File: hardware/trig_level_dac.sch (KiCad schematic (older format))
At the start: 28 parts, among them U701 DAC7563SDSCR, U702 OPA2140

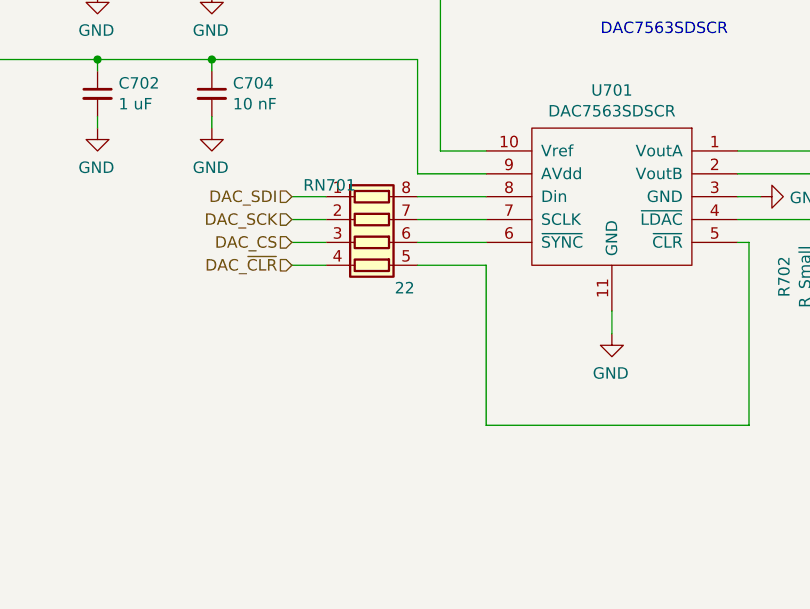
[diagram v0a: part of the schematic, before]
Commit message: work on tdr component placement
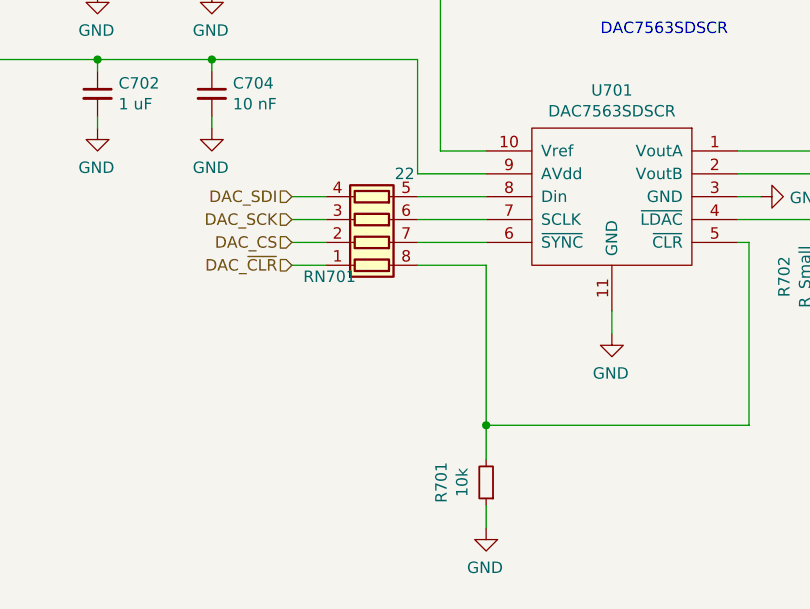
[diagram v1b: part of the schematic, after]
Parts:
- added R701: 10k, Resistors_SMD:R_0402, symbol Device:R_Small
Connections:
- net DAC_CS: now also RN701.2 (R2.1); no longer RN701.3 (R3.1)
- net DAC_SCK: now also RN701.3 (R3.1); no longer RN701.2 (R2.1)
- net DAC_SDI: now also RN701.4 (R4.1); no longer RN701.1 (R1.1)
- net DAC_~CLR: now also RN701.1 (R1.1); no longer RN701.4 (R4.1)
- net GND: now also R701.1
- net at U701.5 (~CLR): now also RN701.8 (R1.2), R701.2; no longer RN701.5 (R4.2)
- net at U701.6 (~SYNC): now also RN701.7 (R2.2); no longer RN701.6 (R3.2)
- net at U701.7 (SCLK): now also RN701.6 (R3.2); no longer RN701.7 (R2.2)
- net at U701.8 (Din): now also RN701.5 (R4.2); no longer RN701.8 (R1.2)
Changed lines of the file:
@@
 L Device:R_Pack04 RN?
 U 1 1 5C28A2D7
-P 2900 4800
+P 2900 4700
 AR Path="/5BC6A656/5C28A2D7" Ref="RN?"  Part="1"
 AR Path="/5BC64E97/5C28A2D7" Ref="RN?"  Part="1"
 AR Path="/5C262FB6/5C28A2D7" Ref="RN701"  Part="1"
-F 0 "RN701" V 2650 4500 50  0000 L CNN
-F 1 "22" V 3100 4900 50  0000 L CNN
-F 2 "Resistors_SMD:R_Array_Convex_4x0402" V 3175 4800 50  0001 C CNN
-F 3 "~" H 2900 4800 50  0001 C CNN
-	1    2900 4800
-	0    1    1    0
+F 0 "RN701" V 2650 4400 50  0000 L CNN
+F 1 "22" V 3100 4800 50  0000 L CNN
+F 2 "Resistors_SMD:R_Array_Convex_4x0402" V 3175 4700 50  0001 C CNN
+F 3 "~" H 2900 4700 50  0001 C CNN
+	1    2900 4700
+	0    1    -1   0
 $EndComp
 Wire Wire Line
@@
 Text HLabel 2550 4900 0    50   Input ~ 0
 DAC_~CLR
+$Comp
+L Device:R_Small R701
+U 1 1 5C36F4E9
+P 3400 5850
+F 0 "R701" V 3596 5850 50  0000 C CNN
+F 1 "10k" V 3505 5850 50  0000 C CNN
+F 2 "Resistors_SMD:R_0402" H 3400 5850 50  0001 C CNN
+F 3 "~" H 3400 5850 50  0001 C CNN
+	1    3400 5850
+	-1   0    0    1
+$EndComp
+$Comp
+L power:GND #PWR0149
+U 1 1 5C36F5ED
+P 3400 6050
+F 0 "#PWR0149" H 3400 5800 50  0001 C CNN
+F 1 "GND" H 3405 5877 50  0000 C CNN
+F 2 "" H 3400 6050 50  0001 C CNN
+F 3 "" H 3400 6050 50  0001 C CNN
+	1    3400 6050
+	-1   0    0    -1
+$EndComp
+Wire Wire Line
+	3400 5600 3400 5750
+Connection ~ 3400 5600
+Wire Wire Line
+	3400 5950 3400 6050
 $EndSCHEMATC

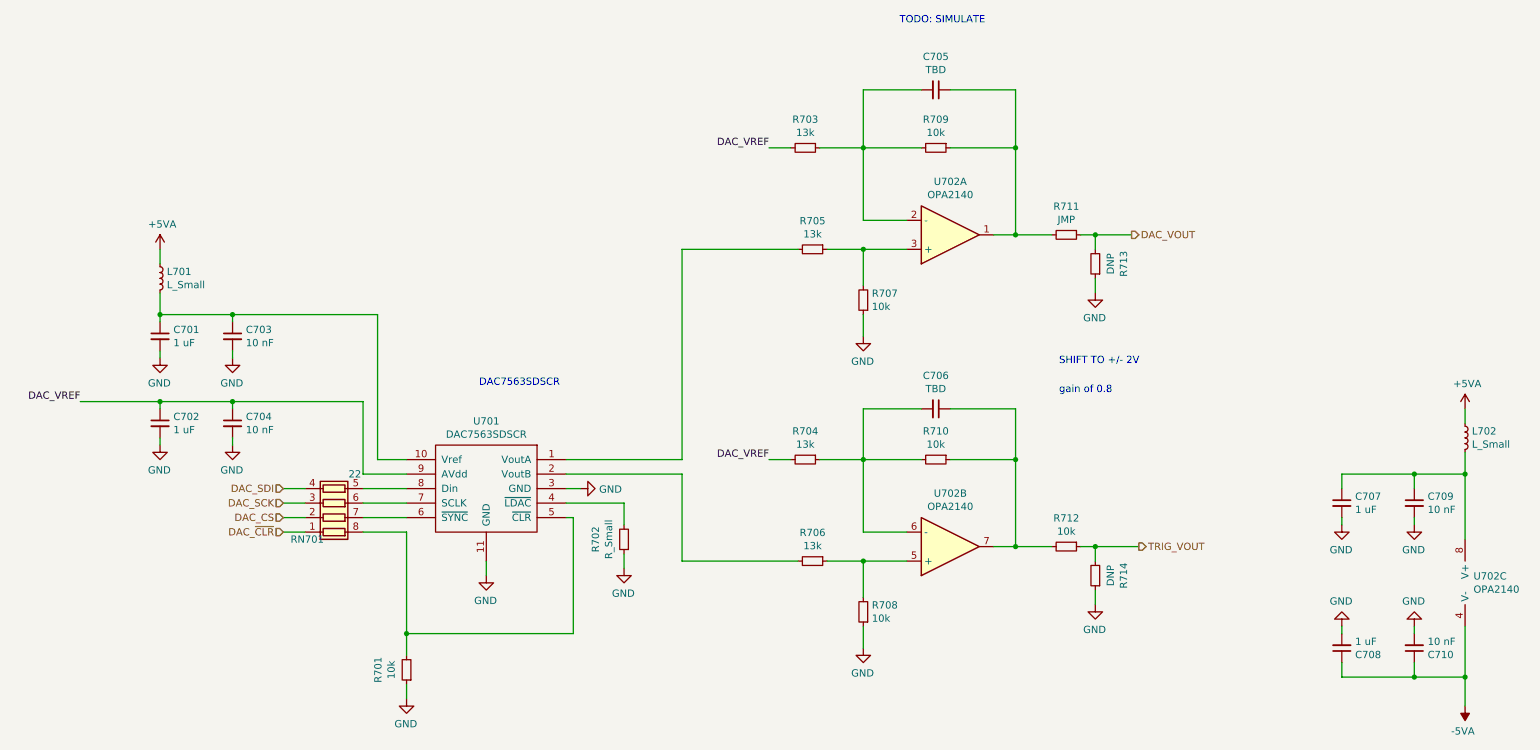
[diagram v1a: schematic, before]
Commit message: schematic cleanup, BOM consolidation
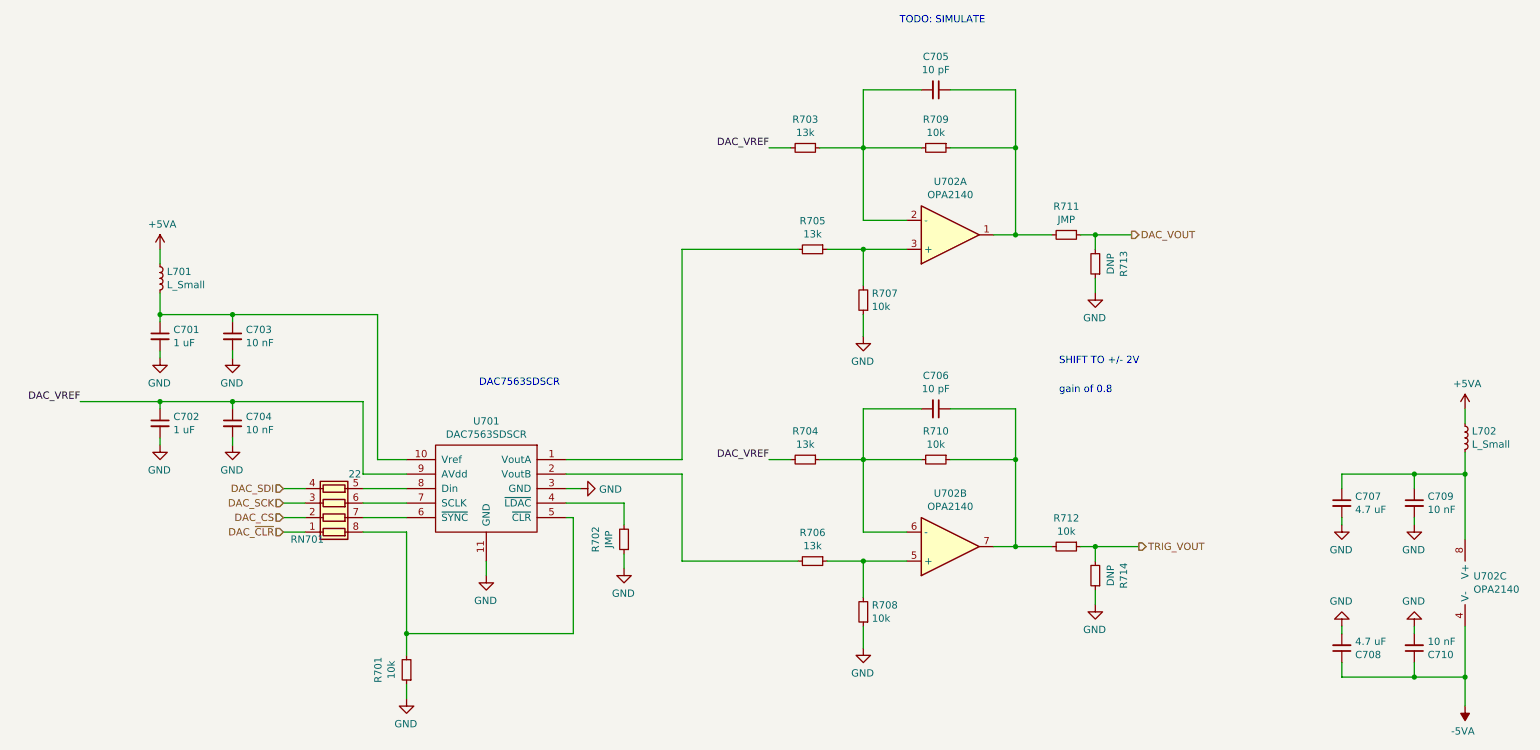
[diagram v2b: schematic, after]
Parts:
- C705, C706: value TBD -> 10 pF
- C707, C708: value 1 uF -> 4.7 uF
- R702: value R_Small -> JMP
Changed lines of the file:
@@
 P 4900 4950
 F 0 "R702" V 5096 4950 50  0000 C CNN
-F 1 "R_Small" V 5005 4950 50  0000 C CNN
+F 1 "JMP" V 5005 4950 50  0000 C CNN
 F 2 "Resistors_SMD:R_0402" H 4900 4950 50  0001 C CNN
 F 3 "~" H 4900 4950 50  0001 C CNN
@@
 P 9850 4700
 F 0 "C707" H 9942 4746 50  0000 L CNN
-F 1 "1 uF" H 9942 4655 50  0000 L CNN
+F 1 "4.7 uF" H 9942 4655 50  0000 L CNN
 F 2 "Capacitors_SMD:C_0603" H 9850 4700 50  0001 C CNN
 F 3 "~" H 9850 4700 50  0001 C CNN
@@
 P 9850 5700
 F 0 "C708" H 9942 5746 50  0000 L CNN
-F 1 "1 uF" H 9942 5655 50  0000 L CNN
+F 1 "4.7 uF" H 9942 5655 50  0000 L CNN
 F 2 "Capacitors_SMD:C_0603" H 9850 5700 50  0001 C CNN
 F 3 "~" H 9850 5700 50  0001 C CNN
@@
 P 7050 1850
 F 0 "C705" V 6821 1850 50  0000 C CNN
-F 1 "TBD" V 6912 1850 50  0000 C CNN
+F 1 "10 pF" V 6912 1850 50  0000 C CNN
 F 2 "Capacitors_SMD:C_0402" H 7050 1850 50  0001 C CNN
 F 3 "~" H 7050 1850 50  0001 C CNN
@@
 P 7050 4050
 F 0 "C706" V 6821 4050 50  0000 C CNN
-F 1 "TBD" V 6912 4050 50  0000 C CNN
+F 1 "10 pF" V 6912 4050 50  0000 C CNN
 F 2 "Capacitors_SMD:C_0402" H 7050 4050 50  0001 C CNN
 F 3 "~" H 7050 4050 50  0001 C CNN

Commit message: assigned pins for tdr beaglebone bitbang driver
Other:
- note added: "TODO: WHAT IS THE STATE OF THIS AT STARTUP?"
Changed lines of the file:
@@
 Wire Wire Line
 	3400 5950 3400 6050
+Text Notes 8200 4300 0    50   ~ 0
+TODO: WHAT IS THE STATE OF THIS AT STARTUP?
 $EndSCHEMATC

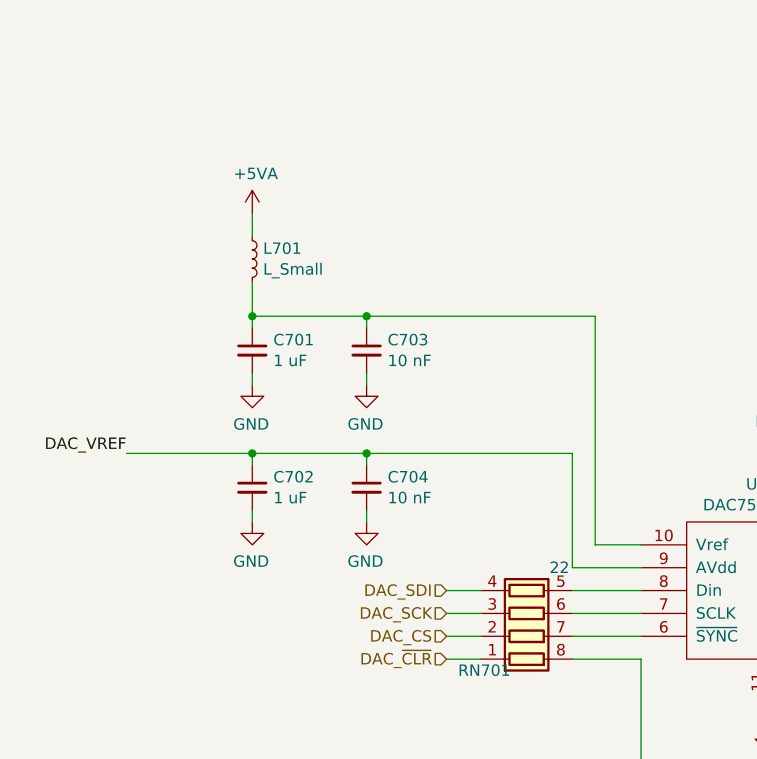
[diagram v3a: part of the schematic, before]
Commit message: fixed U401 and U601 output termination, tdr works, added first sweep of output pulse to README
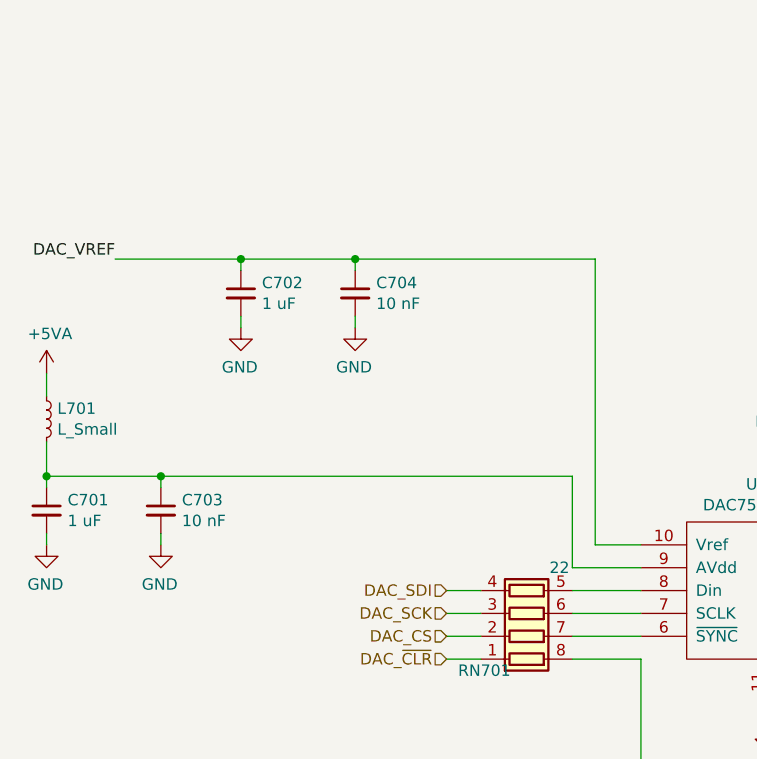
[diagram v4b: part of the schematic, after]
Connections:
- net DAC_VREF: now also U701.10 (Vref); no longer U701.9 (AVdd)
- net at C701.1, C703.1, L701.2: now also U701.9 (AVdd); no longer U701.10 (Vref)
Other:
- moved on the sheet: C701, C702, C703, C704, L701
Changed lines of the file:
@@
 L Device:C_Small C703
 U 1 1 5C28C367
-P 2200 3550
-F 0 "C703" H 2292 3596 50  0000 L CNN
-F 1 "10 nF" H 2292 3505 50  0000 L CNN
-F 2 "Capacitors_SMD:C_0402" H 2200 3550 50  0001 C CNN
-F 3 "~" H 2200 3550 50  0001 C CNN
-	1    2200 3550
+P 1300 4250
+F 0 "C703" H 1392 4296 50  0000 L CNN
+F 1 "10 nF" H 1392 4205 50  0000 L CNN
+F 2 "Capacitors_SMD:C_0402" H 1300 4250 50  0001 C CNN
+F 3 "~" H 1300 4250 50  0001 C CNN
+	1    1300 4250
 	1    0    0    -1
 $EndComp
@@
 L Device:C_Small C701
 U 1 1 5C28C3DD
-P 1700 3550
-F 0 "C701" H 1792 3596 50  0000 L CNN
-F 1 "1 uF" H 1792 3505 50  0000 L CNN
-F 2 "Capacitors_SMD:C_0402" H 1700 3550 50  0001 C CNN
-F 3 "~" H 1700 3550 50  0001 C CNN
-	1    1700 3550
+P 800 4250
+F 0 "C701" H 892 4296 50  0000 L CNN
+F 1 "1 uF" H 892 4205 50  0000 L CNN
+F 2 "Capacitors_SMD:C_0402" H 800 4250 50  0001 C CNN
+F 3 "~" H 800 4250 50  0001 C CNN
+	1    800  4250
 	1    0    0    -1
 $EndComp
@@
 L power:GND #PWR0282
 U 1 1 5C28C8E7
-P 2200 3700
-F 0 "#PWR0282" H 2200 3450 50  0001 C CNN
-F 1 "GND" H 2205 3527 50  0000 C CNN
-F 2 "" H 2200 3700 50  0001 C CNN
-F 3 "" H 2200 3700 50  0001 C CNN
-	1    2200 3700
-	-1   0    0    -1
-$EndComp
-Wire Wire Line
-	1700 3400 2200 3400
-Connection ~ 1700 3400
-Wire Wire Line
-	1700 3400 1700 3450
-Wire Wire Line
-	2200 3400 2200 3450
-Wire Wire Line
-	2200 3650 2200 3700
+P 1300 4400
+F 0 "#PWR0282" H 1300 4150 50  0001 C CNN
+F 1 "GND" H 1305 4227 50  0000 C CNN
+F 2 "" H 1300 4400 50  0001 C CNN
+F 3 "" H 1300 4400 50  0001 C CNN
+	1    1300 4400
+	-1   0    0    -1
+$EndComp
+Wire Wire Line
+	800  4100 1300 4100
+Connection ~ 800  4100
+Wire Wire Line
+	800  4100 800  4150
+Wire Wire Line
+	1300 4100 1300 4150
+Wire Wire Line
+	1300 4350 1300 4400
 $Comp
 L power:GND #PWR0283
 U 1 1 5C28D08C
-P 1700 3700
-F 0 "#PWR0283" H 1700 3450 50  0001 C CNN
-F 1 "GND" H 1705 3527 50  0000 C CNN
-F 2 "" H 1700 3700 50  0001 C CNN
-F 3 "" H 1700 3700 50  0001 C CNN
-	1    1700 3700
-	-1   0    0    -1
-$EndComp
-Wire Wire Line
-	1700 3650 1700 3700
+P 800 4400
+F 0 "#PWR0283" H 800 4150 50  0001 C CNN
+F 1 "GND" H 805 4227 50  0000 C CNN
+F 2 "" H 800 4400 50  0001 C CNN
+F 3 "" H 800 4400 50  0001 C CNN
+	1    800  4400
+	-1   0    0    -1
+$EndComp
+Wire Wire Line
+	800  4350 800  4400
 $Comp
 L Device:C_Small C704
 U 1 1 5C28D757
-P 2200 4150
-F 0 "C704" H 2292 4196 50  0000 L CNN
-F 1 "10 nF" H 2292 4105 50  0000 L CNN
-F 2 "Capacitors_SMD:C_0402" H 2200 4150 50  0001 C CNN
-F 3 "~" H 2200 4150 50  0001 C CNN
-	1    2200 4150
+P 2150 3300
+F 0 "C704" H 2242 3346 50  0000 L CNN
+F 1 "10 nF" H 2242 3255 50  0000 L CNN
+F 2 "Capacitors_SMD:C_0402" H 2150 3300 50  0001 C CNN
+F 3 "~" H 2150 3300 50  0001 C CNN
+	1    2150 3300
 	1    0    0    -1
 $EndComp
@@
 L Device:C_Small C702
 U 1 1 5C28D75E
-P 1700 4150
-F 0 "C702" H 1792 4196 50  0000 L CNN
-F 1 "1 uF" H 1792 4105 50  0000 L CNN
-F 2 "Capacitors_SMD:C_0402" H 1700 4150 50  0001 C CNN
-F 3 "~" H 1700 4150 50  0001 C CNN
-	1    1700 4150
+P 1650 3300
+F 0 "C702" H 1742 3346 50  0000 L CNN
+F 1 "1 uF" H 1742 3255 50  0000 L CNN
+F 2 "Capacitors_SMD:C_0402" H 1650 3300 50  0001 C CNN
+F 3 "~" H 1650 3300 50  0001 C CNN
+	1    1650 3300
 	1    0    0    -1
 $EndComp
@@
 L power:GND #PWR0284
 U 1 1 5C28D765
-P 2200 4300
-F 0 "#PWR0284" H 2200 4050 50  0001 C CNN
-F 1 "GND" H 2205 4127 50  0000 C CNN
-F 2 "" H 2200 4300 50  0001 C CNN
-F 3 "" H 2200 4300 50  0001 C CNN
-	1    2200 4300
-	-1   0    0    -1
-$EndComp
-Wire Wire Line
-	1700 4000 2200 4000
-Wire Wire Line
-	1700 4000 1700 4050
-Wire Wire Line
-	2200 4000 2200 4050
-Wire Wire Line
-	2200 4250 2200 4300
+P 2150 3450
+F 0 "#PWR0284" H 2150 3200 50  0001 C CNN
+F 1 "GND" H 2155 3277 50  0000 C CNN
+F 2 "" H 2150 3450 50  0001 C CNN
+F 3 "" H 2150 3450 50  0001 C CNN
+	1    2150 3450
+	-1   0    0    -1
+$EndComp
+Wire Wire Line
+	1650 3150 2150 3150
+Wire Wire Line
+	1650 3150 1650 3200
+Wire Wire Line
+	2150 3150 2150 3200
+Wire Wire Line
+	2150 3400 2150 3450
 $Comp
 L power:GND #PWR0285
 U 1 1 5C28D771
-P 1700 4300
-F 0 "#PWR0285" H 1700 4050 50  0001 C CNN
-F 1 "GND" H 1705 4127 50  0000 C CNN
-F 2 "" H 1700 4300 50  0001 C CNN
-F 3 "" H 1700 4300 50  0001 C CNN
-	1    1700 4300
-	-1   0    0    -1
-$EndComp
-Wire Wire Line
-	1700 4250 1700 4300
-Wire Wire Line
-	3100 4000 3100 4500
+P 1650 3450
+F 0 "#PWR0285" H 1650 3200 50  0001 C CNN
+F 1 "GND" H 1655 3277 50  0000 C CNN
+F 2 "" H 1650 3450 50  0001 C CNN
+F 3 "" H 1650 3450 50  0001 C CNN
+	1    1650 3450
+	-1   0    0    -1
+$EndComp
+Wire Wire Line
+	1650 3400 1650 3450
 Wire Wire Line
 	3100 4500 3400 4500
-Wire Wire Line
-	2200 4000 3100 4000
-Connection ~ 2200 4000
+Connection ~ 2150 3150
 Wire Wire Line
 	3400 4400 3200 4400
-Wire Wire Line
-	3200 4400 3200 3400
-Wire Wire Line
-	3200 3400 2200 3400
-Connection ~ 2200 3400
+Connection ~ 1300 4100
 $Comp
 L Device:L_Small L701
 U 1 1 5C28FCB9
-P 1700 3150
-F 0 "L701" H 1747 3196 50  0000 L CNN
-F 1 "L_Small" H 1747 3105 50  0000 L CNN
-F 2 "Resistors_SMD:R_0402" H 1700 3150 50  0001 C CNN
-F 3 "~" H 1700 3150 50  0001 C CNN
-	1    1700 3150
-	1    0    0    -1
-$EndComp
-Wire Wire Line
-	1700 3250 1700 3400
-Wire Wire Line
-	1700 2950 1700 3050
+P 800 3850
+F 0 "L701" H 847 3896 50  0000 L CNN
+F 1 "L_Small" H 847 3805 50  0000 L CNN
+F 2 "Resistors_SMD:R_0402" H 800 3850 50  0001 C CNN
+F 3 "~" H 800 3850 50  0001 C CNN
+	1    800  3850
+	1    0    0    -1
+$EndComp
+Wire Wire Line
+	800  3950 800  4100
+Wire Wire Line
+	800  3650 800  3750
 $Comp
 L power:-5VA #PWR?
@@
 L power:+5VA #PWR?
 U 1 1 5C29831C
-P 1700 2950
+P 800 3650
 AR Path="/5BC3F686/5C29831C" Ref="#PWR?"  Part="1"
 AR Path="/5C262FB6/5C29831C" Ref="#PWR0287"  Part="1"
-F 0 "#PWR0287" H 1700 2800 50  0001 C CNN
-F 1 "+5VA" H 1715 3123 50  0000 C CNN
-F 2 "" H 1700 2950 50  0001 C CNN
-F 3 "" H 1700 2950 50  0001 C CNN
-	1    1700 2950
+F 0 "#PWR0287" H 800 3500 50  0001 C CNN
+F 1 "+5VA" H 815 3823 50  0000 C CNN
+F 2 "" H 800 3650 50  0001 C CNN
+F 3 "" H 800 3650 50  0001 C CNN
+	1    800  3650
 	1    0    0    -1
 $EndComp
@@
 	10700 5900 10700 6100
 Connection ~ 10700 5900
-Text Label 1150 4000 2    50   ~ 0
+Text Label 1100 3150 2    50   ~ 0
 DAC_VREF
 Wire Wire Line
-	1150 4000 1700 4000
-Connection ~ 1700 4000
+	1100 3150 1650 3150
+Connection ~ 1650 3150
 Text Label 5900 4400 2    50   ~ 0
 DAC_VREF
@@
 Text Notes 8200 4300 0    50   ~ 0
 TODO: WHAT IS THE STATE OF THIS AT STARTUP?
+Wire Wire Line
+	2150 3150 3200 3150
+Wire Wire Line
+	3200 3150 3200 4400
+Wire Wire Line
+	1300 4100 3100 4100
+Wire Wire Line
+	3100 4100 3100 4500
 $EndSCHEMATC
